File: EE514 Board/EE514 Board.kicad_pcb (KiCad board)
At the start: 2 copper layers, 0 parts

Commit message: Layout finished, updating silkscreen...
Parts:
- added C201: 2.2pF, EE514 Board:C_0603_1608Metric_Pad0.98x0.95mm_HandSolder, F.Cu at (116.4, 117.1)
- added C202: 7.5pF, EE514 Board:C_0603_1608Metric_Pad0.98x0.95mm_HandSolder, F.Cu at (114.5, 113.4)
- added C203: 7.5pF, EE514 Board:C_0603_1608Metric_Pad0.98x0.95mm_HandSolder, F.Cu at (118.3, 116.2)
- added C204: 7.5pF, EE514 Board:C_0603_1608Metric_Pad0.98x0.95mm_HandSolder, F.Cu at (125.8, 116.0)
- added C205: 3.9pF, EE514 Board:C_0603_1608Metric_Pad0.98x0.95mm_HandSolder, F.Cu at (123.0, 118.8)
- added C301: 7.5pF, EE514 Board:C_0603_1608Metric_Pad0.98x0.95mm_HandSolder, F.Cu at (162.4, 93.3)
- added C302: 1pF, EE514 Board:C_1pF_Interdigital, F.Cu at (166.8, 98.6)
- added C303: 1pF, EE514 Board:C_1pF_Interdigital, F.Cu at (169.6, 96.5)
- added C304: 7.5pF, EE514 Board:C_0603_1608Metric_Pad0.98x0.95mm_HandSolder, F.Cu at (171.9, 101.3)
- added C305: 3pF, EE514 Board:C_0603_1608Metric_Pad0.98x0.95mm_HandSolder, F.Cu at (171.0, 98.5)
- added C401: 0.1nF, EE514 Board:C_0603_1608Metric_Pad0.98x0.95mm_HandSolder, F.Cu at (123.3, 102.7)
- added C402: 12nF, EE514 Board:C_0603_1608Metric_Pad0.98x0.95mm_HandSolder, F.Cu at (117.3, 105.5)
- added C403: 0.1nF, EE514 Board:C_0603_1608Metric_Pad0.98x0.95mm_HandSolder, F.Cu at (112.2, 101.1)
- added C404: 12nF, EE514 Board:C_0603_1608Metric_Pad0.98x0.95mm_HandSolder, F.Cu at (125.2, 108.9)
- added C501: 0.1nF, EE514 Board:C_0603_1608Metric_Pad0.98x0.95mm_HandSolder, F.Cu at (147.7, 102.2)
- added C502: 12nF, EE514 Board:C_0603_1608Metric_Pad0.98x0.95mm_HandSolder, F.Cu at (153.2, 96.1)
- added C503: 0.1nF, EE514 Board:C_0603_1608Metric_Pad0.98x0.95mm_HandSolder, F.Cu at (149.4, 91.0)
- added C504: 12nF, EE514 Board:C_0603_1608Metric_Pad0.98x0.95mm_HandSolder, F.Cu at (156.0, 102.2)
- added FL101: BPF-2, EE514 Board:Filter_2.0GHz_Bandpass_Edge-Coupled, F.Cu at (111.3, 78.0)
- added J101: Screw_Terminal_01x02, TerminalBlock_TE-Connectivity:TerminalBlock_TE_282834-2_1x02_P2.54mm_Horizontal, F.Cu at (98.8, 96.3)
- added J102: SMA, Connector_Coaxial:SMA_Molex_73251-1153_EdgeMount_Horizontal, F.Cu at (99.3, 78.0)
- added J103: SMA, Connector_Coaxial:SMA_Molex_73251-1153_EdgeMount_Horizontal, F.Cu at (99.3, 118.1)
- added J104: SMA, Connector_Coaxial:SMA_Molex_73251-1153_EdgeMount_Horizontal, F.Cu at (183.3, 66.3)
- added J105: SMA, Connector_Coaxial:SMA_Molex_73251-1153_EdgeMount_Horizontal, F.Cu at (183.3, 118.1)
- added J106: SMA, Connector_Coaxial:SMA_Molex_73251-1153_EdgeMount_Horizontal, F.Cu at (183.3, 98.5)
- added L201: 2.2nH, EE514 Board:L_0603_1608Metric_Pad0.98x0.95mm_HandSolder, F.Cu at (116.4, 119.9)
- added L202: 18nH, EE514 Board:L_0603_1608Metric_Pad0.98x0.95mm_HandSolder, F.Cu at (116.4, 114.3)
- added L203: 3.9nH, EE514 Board:L_0603_1608Metric_Pad0.98x0.95mm_HandSolder, F.Cu at (123.9, 116.9)
- added L301: 18nH, EE514 Board:L_0603_1608Metric_Pad0.98x0.95mm_HandSolder, F.Cu at (163.4, 96.1)
- added L302: 7.5nH, EE514 Board:L_0603_1608Metric_Pad0.98x0.95mm_HandSolder, F.Cu at (166.2, 96.1)
- added L303: 18nH, EE514 Board:L_0603_1608Metric_Pad0.98x0.95mm_HandSolder, F.Cu at (165.4, 98.0)
- added L304: 18nH, EE514 Board:L_0603_1608Metric_Pad0.98x0.95mm_HandSolder, F.Cu at (171.0, 97.1)
- added L305: 8.2nH, EE514 Board:L_0603_1608Metric_Pad0.98x0.95mm_HandSolder, F.Cu at (170.1, 100.4)
- added Q201: BFP620, EE514 Board:SOT-343_2.0x1.25mm_P1.3mm, F.Cu at (121.1, 117.0)
- added Q301: BPF620, EE514 Board:SOT-343_2.0x1.25mm_P1.3mm, F.Cu at (168.2, 97.6)
- added R201: 1.5, EE514 Board:R_0603_1608Metric_Pad0.98x0.95mm_HandSolder, F.Cu at (118.3, 115.2)
- added R301: 150, EE514 Board:R_0603_1608Metric_Pad0.98x0.95mm_HandSolder, F.Cu at (163.4, 95.2)
- added R401: 1.5k, EE514 Board:R_0603_1608Metric_Pad0.98x0.95mm_HandSolder, F.Cu at (123.3, 106.8)
- added R402: 470, EE514 Board:R_0603_1608Metric_Pad0.98x0.95mm_HandSolder, F.Cu at (123.3, 104.8)
- added R403: 11k, EE514 Board:R_0603_1608Metric_Pad0.98x0.95mm_HandSolder, F.Cu at (122.4, 99.7)
- added R404: 7.4k, EE514 Board:R_0603_1608Metric_Pad0.98x0.95mm_HandSolder, F.Cu at (124.5, 99.7)
- added R405: 3.3k, EE514 Board:R_0603_1608Metric_Pad0.98x0.95mm_HandSolder, F.Cu at (116.4, 108.5)
- added R406: 75, EE514 Board:R_0603_1608Metric_Pad0.98x0.95mm_HandSolder, F.Cu at (122.1, 109.9)
- added R407: 18, EE514 Board:R_0603_1608Metric_Pad0.98x0.95mm_HandSolder, F.Cu at (125.2, 110.9)
- added R501: 1.5k, EE514 Board:R_0603_1608Metric_Pad0.98x0.95mm_HandSolder, F.Cu at (143.7, 102.2)
- added R502: 470, EE514 Board:R_0603_1608Metric_Pad0.98x0.95mm_HandSolder, F.Cu at (145.7, 102.2)
- added R503: 11k, EE514 Board:R_0603_1608Metric_Pad0.98x0.95mm_HandSolder, F.Cu at (150.8, 101.2)
- added R504: 7.4k, EE514 Board:R_0603_1608Metric_Pad0.98x0.95mm_HandSolder, F.Cu at (150.8, 103.2)
- added R505: 3.3k, EE514 Board:R_0603_1608Metric_Pad0.98x0.95mm_HandSolder, F.Cu at (156.8, 95.2)
- added R506: 75, EE514 Board:R_0603_1608Metric_Pad0.98x0.95mm_HandSolder, F.Cu at (158.1, 102.2)
- added R507: 18, EE514 Board:R_0603_1608Metric_Pad0.98x0.95mm_HandSolder, F.Cu at (153.8, 102.2)
- added U401: TLC2201, Package_SO:SOIC-8_3.9x4.9mm_P1.27mm, F.Cu at (117.3, 101.4)
- added U501: TLC2201, Package_SO:SOIC-8_3.9x4.9mm_P1.27mm, F.Cu at (149.1, 96.1)
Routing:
- net +5V: track 0.00 -> 113.5 mm
- net /Amplifier/RF_OUT: track 0.00 -> 62.9 mm
- net GND: track 0.00 -> 52.7 mm, vias 0 -> 27
- net /Bias Regulator (Oscillator)/V_BIAS_COLLECTOR: track 0.00 -> 31.6 mm
- net /Amplifier/V_BIAS_COLLECTOR: track 0.00 -> 24.5 mm
- net /FILT_IN: track 0.00 -> 23.9 mm
- net /FILT_OUT: track 0.00 -> 23.1 mm
- net /Amplifier/RF_IN: track 0.00 -> 19.8 mm
- net /Bias Regulator (Oscillator)/VREF_1.2V: track 0.00 -> 13.2 mm
- net /Bias Regulator (Amplifier)/VREF_1.2V: track 0.00 -> 11.8 mm
- net /Oscillator/RF_OUT: track 0.00 -> 10.4 mm
- net Net-(C402-Pad1): track 0.00 -> 8.20 mm
- net Net-(C502-Pad1): track 0.00 -> 7.42 mm
- net /Bias Regulator (Oscillator)/V_BIAS_BASE: track 0.00 -> 6.64 mm
- net /Amplifier/V_BIAS_BASE: track 0.00 -> 4.96 mm
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- added copper zone on F.Cu, net /Amplifier/RF_IN
- added copper zone on F.Cu, net /Amplifier/RF_OUT
- added copper zone on F.Cu, net /FILT_IN
- added copper zone on F.Cu, net /FILT_OUT
- added copper zone on F.Cu, net /Oscillator/RF_OUT
- added copper zone on B.Cu, net GND
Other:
- board outline added: 93 x 69.9 mm
- net class Default: clearance 0.2 -> 0.2032; trace_width 0.25 -> 0.3048
- rule trace_clearance: 0.2 -> 0.2032

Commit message: Finished placing silkscreen
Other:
- board text added: "2.0 GHz Amplifier"
- board text added: "2.0 GHz Oscillator"
- board text added: "2.0GHz Band-Pass Filter"
- board text added: "DC Bias Regulators"

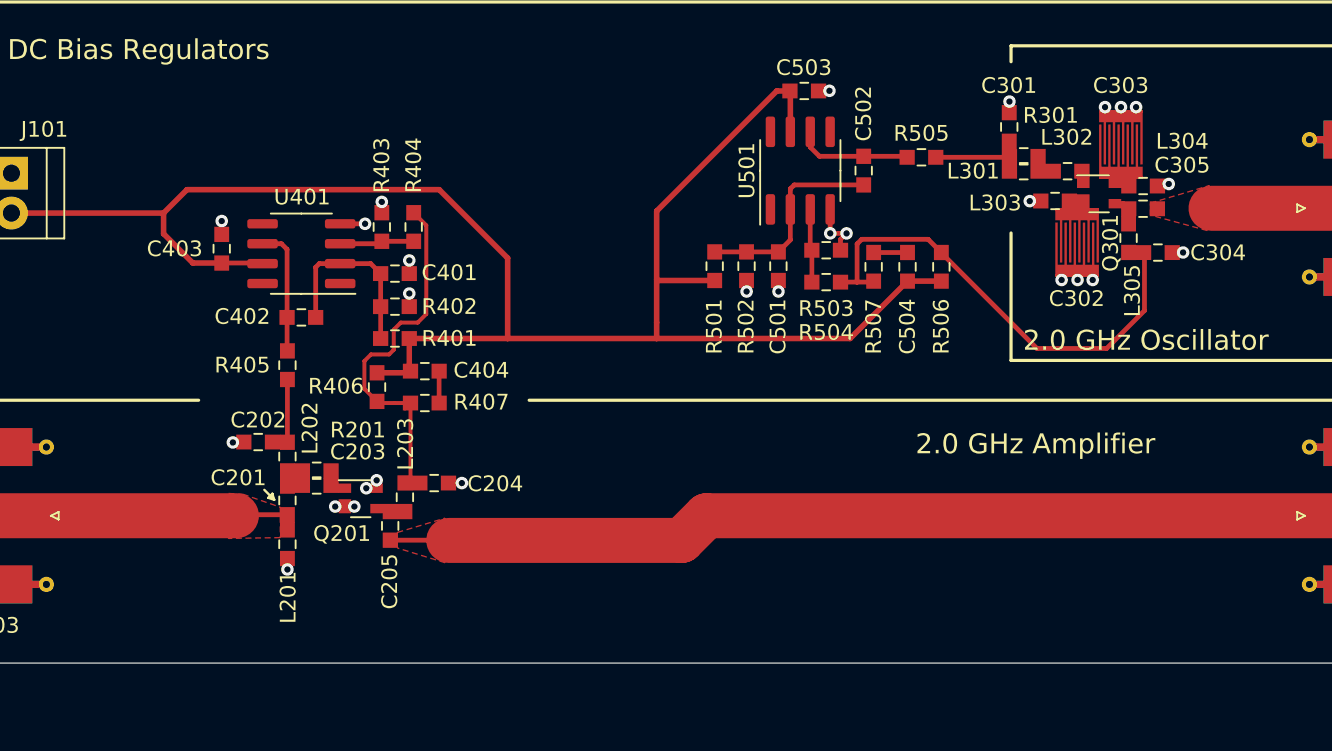
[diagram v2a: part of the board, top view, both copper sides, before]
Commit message: Added silkscreen and logo
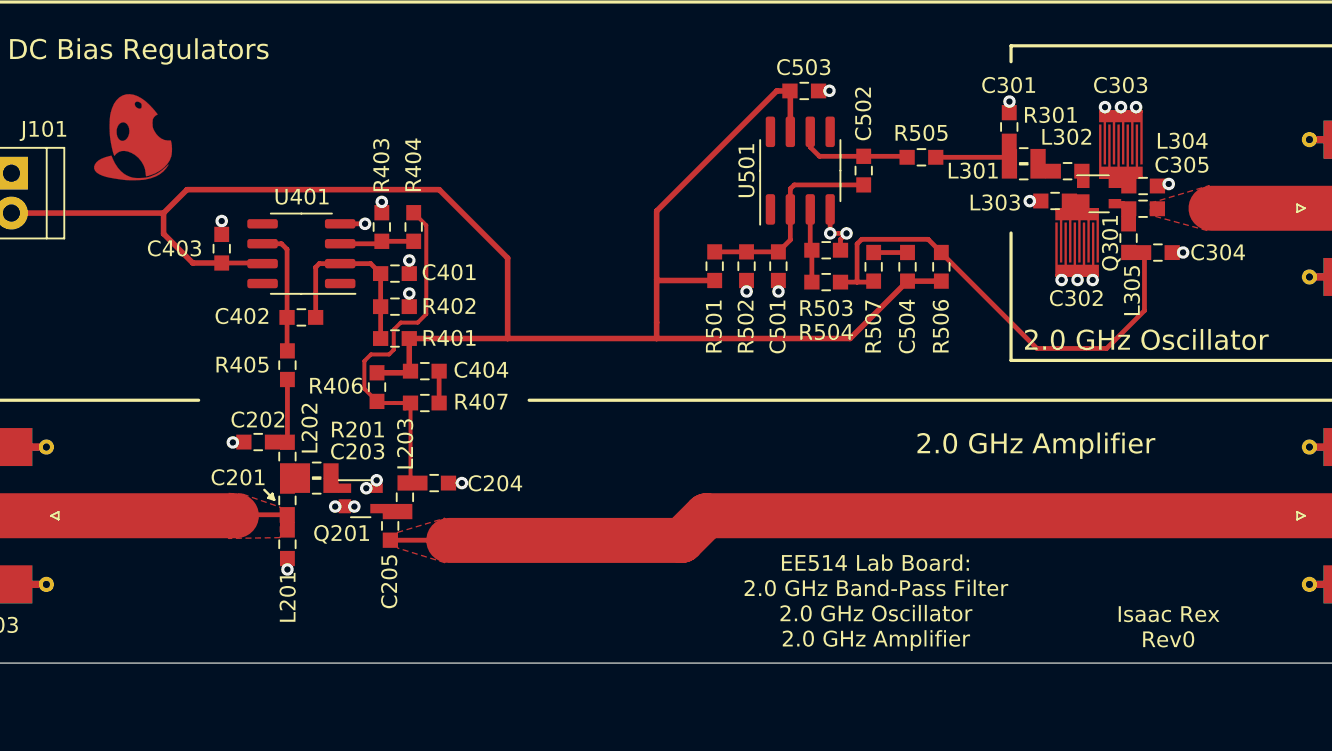
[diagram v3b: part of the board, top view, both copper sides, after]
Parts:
- added G***: IREX_LOGO, irex_Aesthetic:Logo_irex_5.0x5.5mm_Copper, F.Cu at (106.6, 94.0)
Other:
- board text added: "EE514 Lab Board: 2.0 GHz Band-Pass Filter 2.0 GHz Oscillator 2.0 GHz Amplifier"
- board text added: "Isaac Rex Rev0"

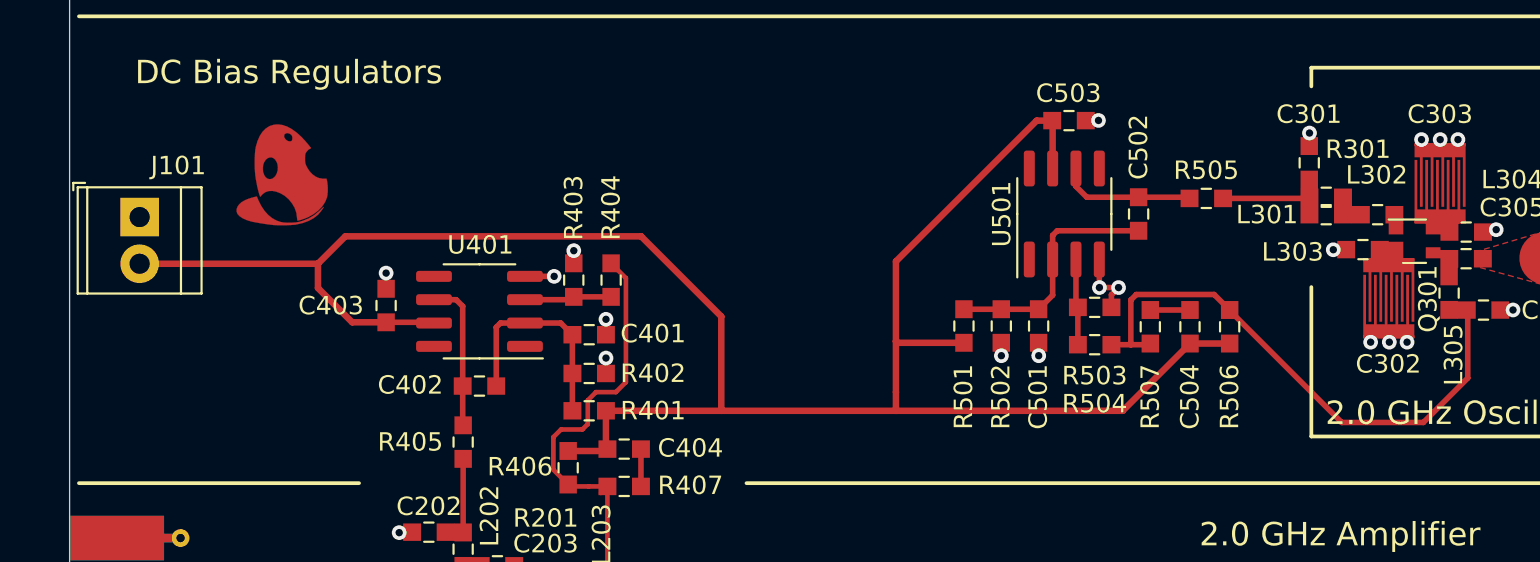
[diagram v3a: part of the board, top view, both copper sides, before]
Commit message: Updated soldermask on interdigital cap, added silkscreen for DC terminal, updated gerbers
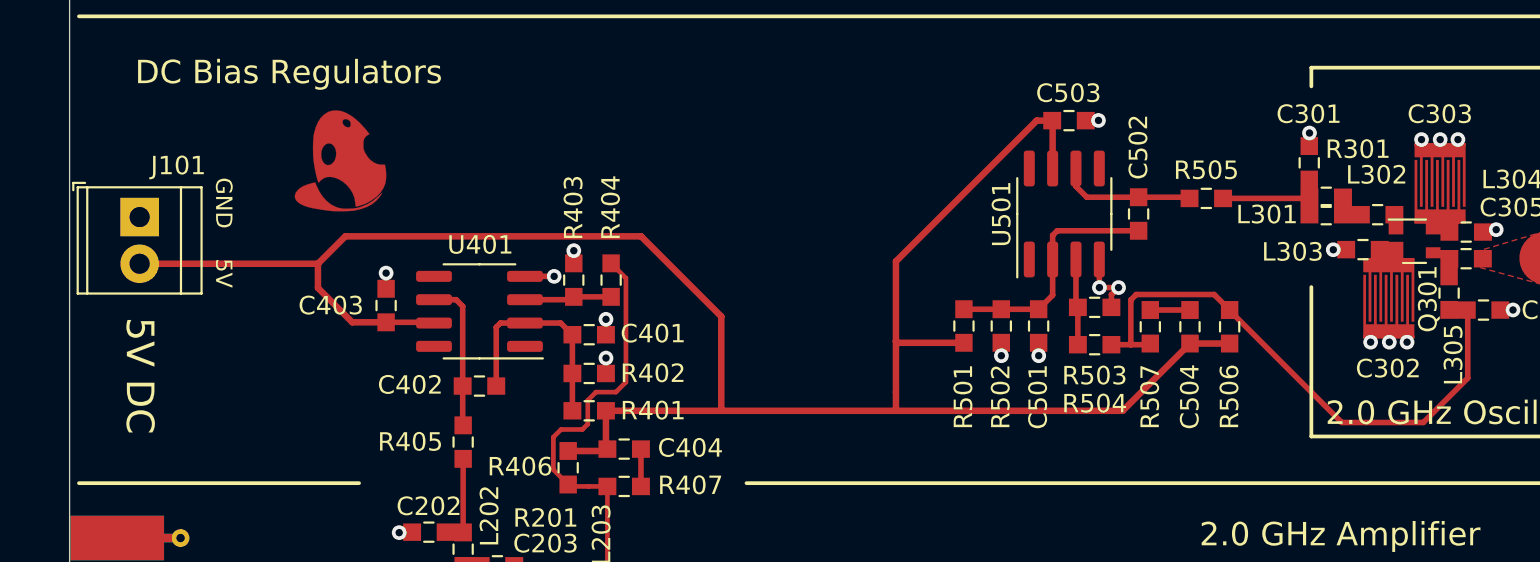
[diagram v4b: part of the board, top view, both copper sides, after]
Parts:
- moved G*** 3.27 mm to (109.7, 93.2)
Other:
- board text added: "5V"
- board text added: "5V DC"
- board text added: "GND"
